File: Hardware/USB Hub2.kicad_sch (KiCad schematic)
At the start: 62 parts, among them J1 Conn_01x07_Male, J10 Conn_01x04_Male, J11 USB_C_Receptacle, J12 USB_C_Receptacle, J2 Conn_01x04_Male, J3 Conn_01x02_Male, J4 Conn_01x02_Male, J5 Conn_01x02_Male, J6 Conn_01x02_Male, J7 Conn_01x08_Male, J8 QWIIC_Vertical, J9 QWIIC_Stack_II, U1 TUSB2036, U2 AP2112K-3.3, U3 TPS2550DBVTG4, U4 TPS2550DBVTG4, U5 TPS2550DBVTG4, X1 ASE-xxxMHz

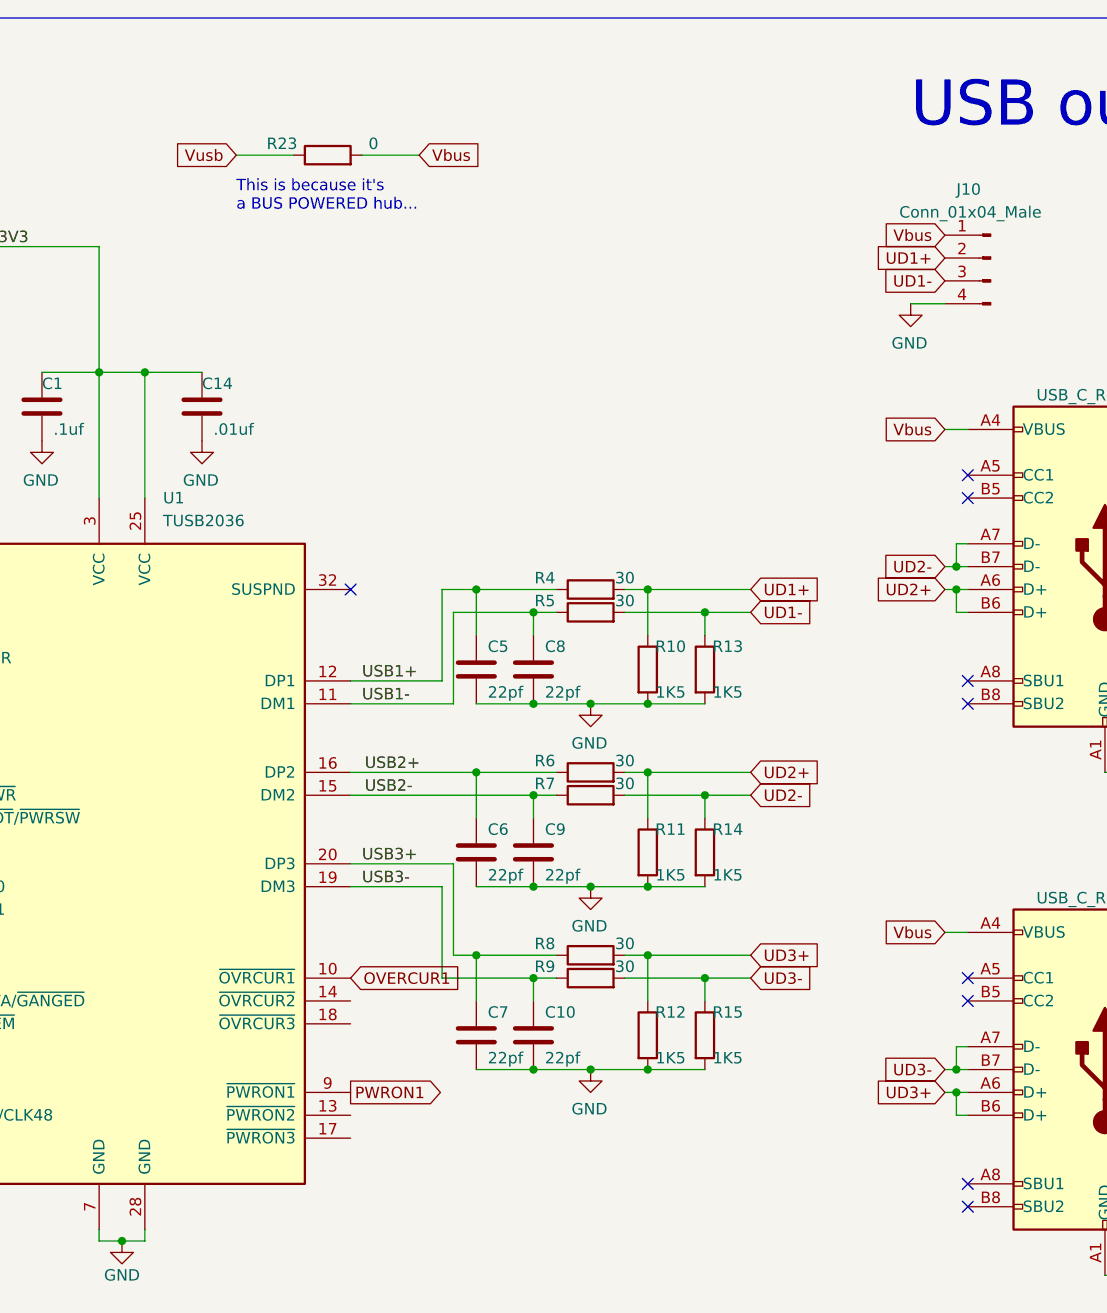
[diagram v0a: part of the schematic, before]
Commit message: USB Hub2... Now with Overcurrent Protection
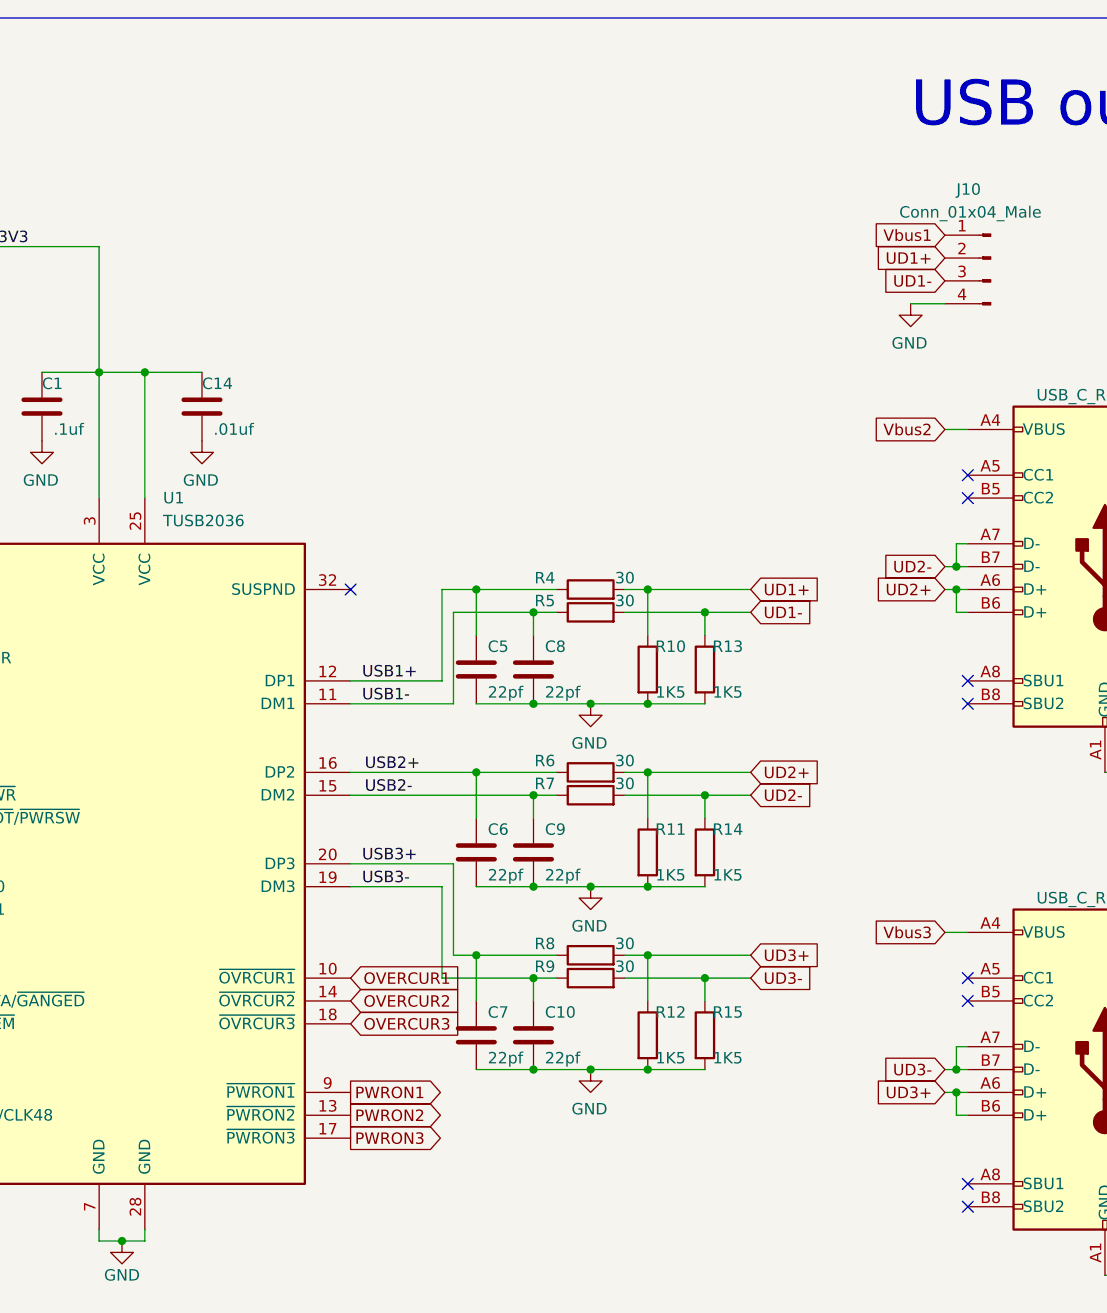
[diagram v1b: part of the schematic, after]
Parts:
- removed R23: 0, Resistor_SMD:R_0603_1608Metric, symbol Device:R
- U3: footprint Package_TO_SOT_SMD:SOT-23-6 -> Tinker:SOT-23-6
- U4, U5: footprint (none) -> Tinker:SOT-23-6
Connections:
- net OVERCUR2: now also U1.14 (~{OVRCUR2})
- net OVERCUR3: now also U1.18 (~{OVRCUR3})
- net PWRON2: now also U1.13 (~{PWRON2})
- net PWRON3: now also U1.17 (~{PWRON3})
- net Vbus1: now also J10.1 (Pin_1)
- net Vbus2: now also J11.A4 (VBUS), J11.A9 (VBUS), J11.B4 (VBUS), J11.B9 (VBUS)
- net Vbus3: now also J12.A4 (VBUS), J12.A9 (VBUS), J12.B4 (VBUS), J12.B9 (VBUS)
- removed net Vbus: J10.1 (Pin_1), J11.A4 (VBUS), J11.A9 (VBUS), J11.B4 (VBUS), J11.B9 (VBUS), J12.A4 (VBUS), J12.A9 (VBUS), J12.B4 (VBUS), J12.B9 (VBUS)
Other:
- note removed: "This is because it's a BUS POWERED hub..."

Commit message: More about the Hub...
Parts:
- added D5, D6, D7, D8: PGB1010603NR, Tinker:PGB1010603NRHF, symbol PGB1010603NR:PGB1010603NR
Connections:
- net CC1 is gone; now on net UD1-: D3.1
- net CC2 is gone; now on net UD1+: D4.1
- net GND: now also D5.2, D6.2, D7.2, D8.2
- net UD2+: now also D6.1
- net UD2-: now also D5.1
- net UD3+: now also D8.1
- net UD3-: now also D7.1
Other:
- moved on the sheet: D3, D4

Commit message: Still... USB Hub...
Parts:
- added JP1: Jumper_3_Bridged12, Jumper:SolderJumper-3_P1.3mm_Bridged2Bar12_RoundedPad1.0x1.5mm, symbol Jumper:Jumper_3_Bridged12
- added JP2: Jumper_3_Bridged12, Jumper:SolderJumper-3_P1.3mm_Bridged12_RoundedPad1.0x1.5mm, symbol Jumper:Jumper_3_Bridged12
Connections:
- net +3V3: now also U1.6 (EEDATA/~{GANGED}), JP2.3 (B)
- net GND: now also JP2.1 (A); no longer U1.8 (~{BUSPWR})
- net Vsec: now also J5.1 (Pin_1), J6.1 (Pin_1), JP1.3 (B)
- net Vusb: now also JP1.1 (A); no longer C12.1, C15.1, C16.1, C17.1, R17.1, R18.1, R19.1, U2.1 (VIN), U2.3 (EN), U3.1 (IN), U4.1 (IN), U5.1 (IN)
- new net Vusb_PWR: C12.1, C15.1, C16.1, C17.1, JP1.2 (C), R17.1, R18.1, R19.1, U2.1 (VIN), U2.3 (EN), U3.1 (IN), U4.1 (IN), U5.1 (IN)
- new net ~{BUSPWR}: JP2.2 (C), U1.8 (~{BUSPWR})
- no-connect marks 12 -> 11

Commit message: USB Hub2 is pretty much complete!
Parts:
- X1: value ASE-xxxMHz -> ASE-48.000MHz
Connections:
- net XTAL1 renamed CLK48
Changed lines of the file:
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@@
   (junction (at 210.82 90.17) (diameter 0) (color 0 0 0 0)
   )
+  (junction (at 132.08 113.03) (diameter 0) (color 0 0 0 0)
+  )
   (junction (at 251.46 133.35) (diameter 0) (color 0 0 0 0)
   )
@@
   (junction (at 320.04 123.19) (diameter 0) (color 0 0 0 0)
   )
+  (junction (at 132.08 110.49) (diameter 0) (color 0 0 0 0)
+  )
   (junction (at 198.12 77.47) (diameter 0) (color 0 0 0 0)
   )
@@
   (junction (at 320.04 31.75) (diameter 0) (color 0 0 0 0)
   )
-  (junction (at 128.27 110.49) (diameter 0) (color 0 0 0 0)
-  )
-  (junction (at 128.27 113.03) (diameter 0) (color 0 0 0 0)
-  )
   (junction (at 135.89 39.37) (diameter 0) (color 0 0 0 0)
   )
@@
   (no_connect (at 133.35 120.65))
   (no_connect (at 252.73 87.63))
-  (wire (pts (xy 128.27 107.95) (xy 128.27 110.49))
+  (wire (pts (xy 132.08 107.95) (xy 132.08 110.49))
     (stroke (width 0) (type default) (color 0 0 0 0))
   )
@@
     (stroke (width 0) (type default) (color 0 0 0 0))
   )
+  (wire (pts (xy 132.08 113.03) (xy 133.35 113.03))
+    (stroke (width 0) (type default) (color 0 0 0 0))
+  )
   (wire (pts (xy 223.52 100.33) (xy 223.52 102.87))
     (stroke (width 0) (type default) (color 0 0 0 0))
@@
     (stroke (width 0) (type default) (color 0 0 0 0))
   )
-  (wire (pts (xy 128.27 110.49) (xy 133.35 110.49))
-    (stroke (width 0) (type default) (color 0 0 0 0))
-  )
   (wire (pts (xy 335.28 137.16) (xy 370.84 137.16))
     (stroke (width 0) (type default) (color 0 0 0 0))
@@
     (stroke (width 0) (type default) (color 0 0 0 0))
   )
-  (wire (pts (xy 128.27 100.33) (xy 128.27 106.68))
+  (wire (pts (xy 128.27 100.33) (xy 128.27 109.22))
     (stroke (width 0) (type default) (color 0 0 0 0))
   )
@@
     (stroke (width 0) (type default) (color 0 0 0 0))
   )
-  (wire (pts (xy 125.73 106.68) (xy 125.73 109.22))
-    (stroke (width 0) (type default) (color 0 0 0 0))
-  )
   (wire (pts (xy 195.58 80.01) (xy 204.47 80.01))
     (stroke (width 0) (type default) (color 0 0 0 0))
   )
-  (wire (pts (xy 128.27 110.49) (xy 128.27 113.03))
+  (wire (pts (xy 132.08 110.49) (xy 132.08 113.03))
     (stroke (width 0) (type default) (color 0 0 0 0))
   )
@@
     (stroke (width 0) (type default) (color 0 0 0 0))
   )
-  (wire (pts (xy 123.19 109.22) (xy 125.73 109.22))
+  (wire (pts (xy 106.68 109.22) (xy 128.27 109.22))
     (stroke (width 0) (type default) (color 0 0 0 0))
   )
@@
     (stroke (width 0) (type default) (color 0 0 0 0))
   )
-  (wire (pts (xy 128.27 107.95) (xy 133.35 107.95))
+  (wire (pts (xy 132.08 107.95) (xy 133.35 107.95))
     (stroke (width 0) (type default) (color 0 0 0 0))
   )
@@
     (stroke (width 0) (type default) (color 0 0 0 0))
   )
+  (wire (pts (xy 132.08 110.49) (xy 133.35 110.49))
+    (stroke (width 0) (type default) (color 0 0 0 0))
+  )
   (wire (pts (xy 66.04 67.31) (xy 57.15 67.31))
     (stroke (width 0) (type default) (color 0 0 0 0))
@@
     (stroke (width 0) (type default) (color 0 0 0 0))
   )
-  (wire (pts (xy 128.27 113.03) (xy 133.35 113.03))
-    (stroke (width 0) (type default) (color 0 0 0 0))
-  )
   (wire (pts (xy 223.52 120.65) (xy 228.6 120.65))
     (stroke (width 0) (type default) (color 0 0 0 0))
@@
     (stroke (width 0) (type default) (color 0 0 0 0))
   )
-  (wire (pts (xy 128.27 106.68) (xy 125.73 106.68))
-    (stroke (width 0) (type default) (color 0 0 0 0))
-  )
   (wire (pts (xy 267.97 97.79) (xy 271.78 97.79))
     (stroke (width 0) (type default) (color 0 0 0 0))
@@
     (effects (font (size 1.27 1.27)) (justify left bottom))
   )
-  (label "XTAL1" (at 128.27 135.89 0)
+  (label "CLK48" (at 128.27 135.89 0)
     (effects (font (size 1.27 1.27)) (justify left bottom))
   )
@@
     )
   )
-  (global_label "~{BUSPWR}" (shape input) (at 123.19 109.22 180) (fields_autoplaced)
+  (global_label "~{BUSPWR}" (shape input) (at 106.68 109.22 180) (fields_autoplaced)
     (effects (font (size 1.27 1.27)) (justify right))
-    (property "Intersheet References" "${INTERSHEET_REFS}" (id 0) (at 112.9755 109.1406 0)
+    (property "Intersheet References" "${INTERSHEET_REFS}" (id 0) (at 96.4655 109.1406 0)
       (effects (font (size 1.27 1.27)) (justify right) hide)
     )
@@
   )
   (symbol (lib_id "PGB1010603NR:PGB1010603NR") (at 393.7 166.37 0) (unit 1)
-    (in_bom yes) (on_board no)
+    (in_bom yes) (on_board yes)
     (property "Reference" "D5" (id 0) (at 403.86 162.56 0))
     (property "Value" "PGB1010603NR" (id 1) (at 403.86 170.18 0))
@@
   )
   (symbol (lib_id "PGB1010603NR:PGB1010603NR") (at 355.6 166.37 0) (unit 1)
-    (in_bom yes) (on_board no)
+    (in_bom yes) (on_board yes)
     (property "Reference" "D3" (id 0) (at 365.76 162.56 0))
     (property "Value" "PGB1010603NR" (id 1) (at 365.76 170.18 0))
@@
     (pin "2")
   )
-  (symbol (lib_id "power:GND") (at 128.27 113.03 0) (mirror y) (unit 1)
+  (symbol (lib_id "power:GND") (at 132.08 113.03 0) (mirror y) (unit 1)
     (in_bom yes) (on_board yes)
-    (property "Reference" "#PWR0122" (id 0) (at 128.27 119.38 0)
+    (property "Reference" "#PWR0122" (id 0) (at 132.08 119.38 0)
       (effects (font (size 1.27 1.27)) hide)
     )
-    (property "Value" "GND" (id 1) (at 128.27 116.84 0))
-    (property "Footprint" "" (id 2) (at 128.27 113.03 0)
+    (property "Value" "GND" (id 1) (at 132.08 116.84 0))
+    (property "Footprint" "" (id 2) (at 132.08 113.03 0)
       (effects (font (size 1.27 1.27)) hide)
     )
-    (property "Datasheet" "" (id 3) (at 128.27 113.03 0)
+    (property "Datasheet" "" (id 3) (at 132.08 113.03 0)
       (effects (font (size 1.27 1.27)) hide)
     )
@@
   )
   (symbol (lib_id "PGB1010603NR:PGB1010603NR") (at 393.7 176.53 0) (unit 1)
-    (in_bom yes) (on_board no)
+    (in_bom yes) (on_board yes)
     (property "Reference" "D6" (id 0) (at 403.86 172.72 0))
     (property "Value" "PGB1010603NR" (id 1) (at 403.86 180.34 0))
@@
     (in_bom yes) (on_board yes)
     (property "Reference" "X1" (id 0) (at 129.54 147.32 0))
-    (property "Value" "ASE-xxxMHz" (id 1) (at 132.08 149.86 0))
+    (property "Value" "ASE-48.000MHz" (id 1) (at 132.08 149.86 0))
     (property "Footprint" "Oscillator:Oscillator_SMD_Abracon_ASE-4Pin_3.2x2.5mm" (id 2) (at 138.43 149.86 0)
       (effects (font (size 1.27 1.27)) hide)
@@
   )
   (symbol (lib_id "PGB1010603NR:PGB1010603NR") (at 355.6 176.53 0) (unit 1)
-    (in_bom yes) (on_board no)
+    (in_bom yes) (on_board yes)
     (property "Reference" "D4" (id 0) (at 365.76 172.72 0))
     (property "Value" "PGB1010603NR" (id 1) (at 365.76 180.34 0))
@@
   )
   (symbol (lib_id "PGB1010603NR:PGB1010603NR") (at 431.8 176.53 0) (unit 1)
-    (in_bom yes) (on_board no)
+    (in_bom yes) (on_board yes)
     (property "Reference" "D8" (id 0) (at 441.96 172.72 0))
     (property "Value" "PGB1010603NR" (id 1) (at 441.96 180.34 0))
@@
   )
   (symbol (lib_id "PGB1010603NR:PGB1010603NR") (at 431.8 166.37 0) (unit 1)
-    (in_bom yes) (on_board no)
+    (in_bom yes) (on_board yes)
     (property "Reference" "D7" (id 0) (at 441.96 162.56 0))
     (property "Value" "PGB1010603NR" (id 1) (at 441.96 170.18 0))
@@
     )
     (path "/e2bbfb5c-6df7-4fc7-80b6-771dc8b63db1"
-      (reference "X1") (unit 1) (value "ASE-xxxMHz") (footprint "Oscillator:Oscillator_SMD_Abracon_ASE-4Pin_3.2x2.5mm")
+      (reference "X1") (unit 1) (value "ASE-48.000MHz") (footprint "Oscillator:Oscillator_SMD_Abracon_ASE-4Pin_3.2x2.5mm")
     )
   )

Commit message: Yay fer Hub2!
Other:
- moved on the sheet: C15, C16, C17, D1, D2, D3, D4, D5, D6, D7, D8, JP1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

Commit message: s'more work on the hub
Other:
- note removed: "LCSC: C10677"
- moved on the sheet: D1, D2, D3, D4, D5, D6, D7, D8, JP1, JP2
